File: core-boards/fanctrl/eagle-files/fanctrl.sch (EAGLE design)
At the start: 31 parts, among them J1 3-PIN_2MM-H, U1 MCP9701T-E/TT

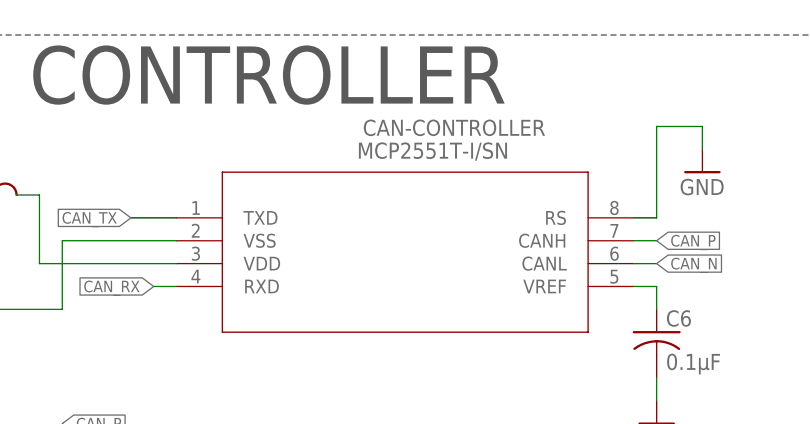
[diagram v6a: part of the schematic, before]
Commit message: Change CAN controller name to MCP2551.
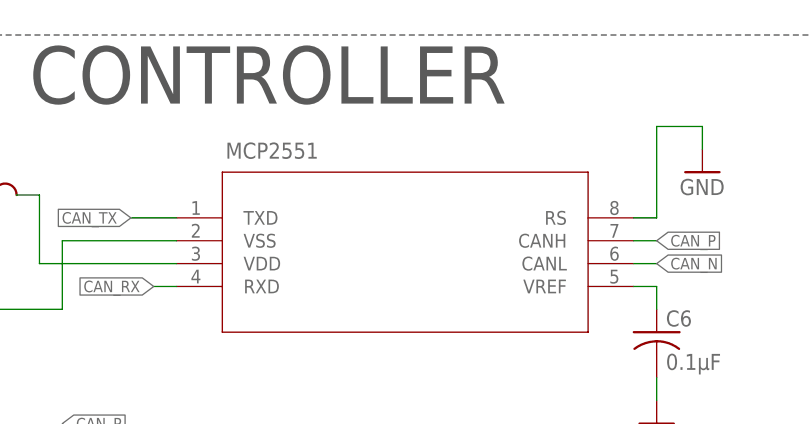
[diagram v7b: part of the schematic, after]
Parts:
- renumbered CAN-CONTROLLER to MCP2551
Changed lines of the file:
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@@
 <part name="P+6" library="supply1" library_urn="urn:adsk.eagle:library:371" deviceset="+5V" device=""/>
 <part name="GND11" library="supply1" library_urn="urn:adsk.eagle:library:371" deviceset="GND" device=""/>
-<part name="CAN-CONTROLLER" library="IGVC-Microcontroller" deviceset="MCP2551T-I/SN" device=""/>
+<part name="MCP2551" library="IGVC-Microcontroller" deviceset="MCP2551T-I/SN" device=""/>
 <part name="C5" library="rcl" library_urn="urn:adsk.eagle:library:334" deviceset="C-US" device="C0603" package3d_urn="urn:adsk.eagle:package:23616/2" value="0.1µF"/>
 <part name="GND12" library="supply1" library_urn="urn:adsk.eagle:library:371" deviceset="GND" device=""/>
@@
 <attribute name="VALUE" x="43.18" y="165.1" size="1.778" layer="96"/>
 </instance>
-<instance part="CAN-CONTROLLER" gate="A" x="190.5" y="187.96" smashed="yes">
-<attribute name="NAME" x="213.7156" y="197.0786" size="1.778" layer="95" rot="SR0"/>
-<attribute name="VALUE" x="213.0806" y="194.5386" size="1.778" layer="96" rot="SR0"/>
+<instance part="MCP2551" gate="A" x="190.5" y="187.96" smashed="yes">
+<attribute name="NAME" x="198.4756" y="194.5386" size="1.778" layer="95" rot="SR0"/>
 </instance>
 <instance part="C5" gate="G$1" x="162.56" y="185.42" smashed="yes">
@@
 </segment>
 <segment>
-<pinref part="CAN-CONTROLLER" gate="A" pin="VSS"/>
+<pinref part="MCP2551" gate="A" pin="VSS"/>
 <wire x1="193.04" y1="185.42" x2="180.34" y2="185.42" width="0.1524" layer="91"/>
 <wire x1="180.34" y1="185.42" x2="180.34" y2="177.8" width="0.1524" layer="91"/>
@@
 </segment>
 <segment>
-<pinref part="CAN-CONTROLLER" gate="A" pin="RS"/>
+<pinref part="MCP2551" gate="A" pin="RS"/>
 <wire x1="243.84" y1="187.96" x2="246.38" y2="187.96" width="0.1524" layer="91"/>
 <wire x1="246.38" y1="187.96" x2="246.38" y2="198.12" width="0.1524" layer="91"/>
@@
 <net name="VREF" class="0">
 <segment>
-<pinref part="CAN-CONTROLLER" gate="A" pin="VREF"/>
+<pinref part="MCP2551" gate="A" pin="VREF"/>
 <wire x1="243.84" y1="180.34" x2="246.38" y2="180.34" width="0.1524" layer="91"/>
 <wire x1="246.38" y1="180.34" x2="246.38" y2="177.8" width="0.1524" layer="91"/>
@@
 <net name="CAN_P" class="0">
 <segment>
-<pinref part="CAN-CONTROLLER" gate="A" pin="CANH"/>
+<pinref part="MCP2551" gate="A" pin="CANH"/>
 <wire x1="243.84" y1="185.42" x2="246.38" y2="185.42" width="0.1524" layer="91"/>
 <label x="246.38" y="185.42" size="1.27" layer="95" font="vector" xref="yes"/>
@@
 <net name="CAN_N" class="0">
 <segment>
-<pinref part="CAN-CONTROLLER" gate="A" pin="CANL"/>
+<pinref part="MCP2551" gate="A" pin="CANL"/>
 <wire x1="243.84" y1="182.88" x2="246.38" y2="182.88" width="0.1524" layer="91"/>
 <label x="246.38" y="182.88" size="1.27" layer="95" font="vector" xref="yes"/>
@@
 <net name="CAN_TX" class="0">
 <segment>
-<pinref part="CAN-CONTROLLER" gate="A" pin="TXD"/>
+<pinref part="MCP2551" gate="A" pin="TXD"/>
 <wire x1="193.04" y1="187.96" x2="187.96" y2="187.96" width="0.1524" layer="91"/>
 <label x="187.96" y="187.96" size="1.27" layer="95" font="vector" rot="R180" xref="yes"/>
@@
 <net name="CAN_RX" class="0">
 <segment>
-<pinref part="CAN-CONTROLLER" gate="A" pin="RXD"/>
+<pinref part="MCP2551" gate="A" pin="RXD"/>
 <wire x1="193.04" y1="180.34" x2="190.5" y2="180.34" width="0.1524" layer="91"/>
 <label x="190.5" y="180.34" size="1.27" layer="95" font="vector" rot="R180" xref="yes"/>
@@
 <net name="+5V_UNFUSED" class="0">
 <segment>
-<pinref part="CAN-CONTROLLER" gate="A" pin="VDD"/>
+<pinref part="MCP2551" gate="A" pin="VDD"/>
 <wire x1="193.04" y1="182.88" x2="177.8" y2="182.88" width="0.1524" layer="91"/>
 <wire x1="177.8" y1="182.88" x2="177.8" y2="190.5" width="0.1524" layer="91"/>

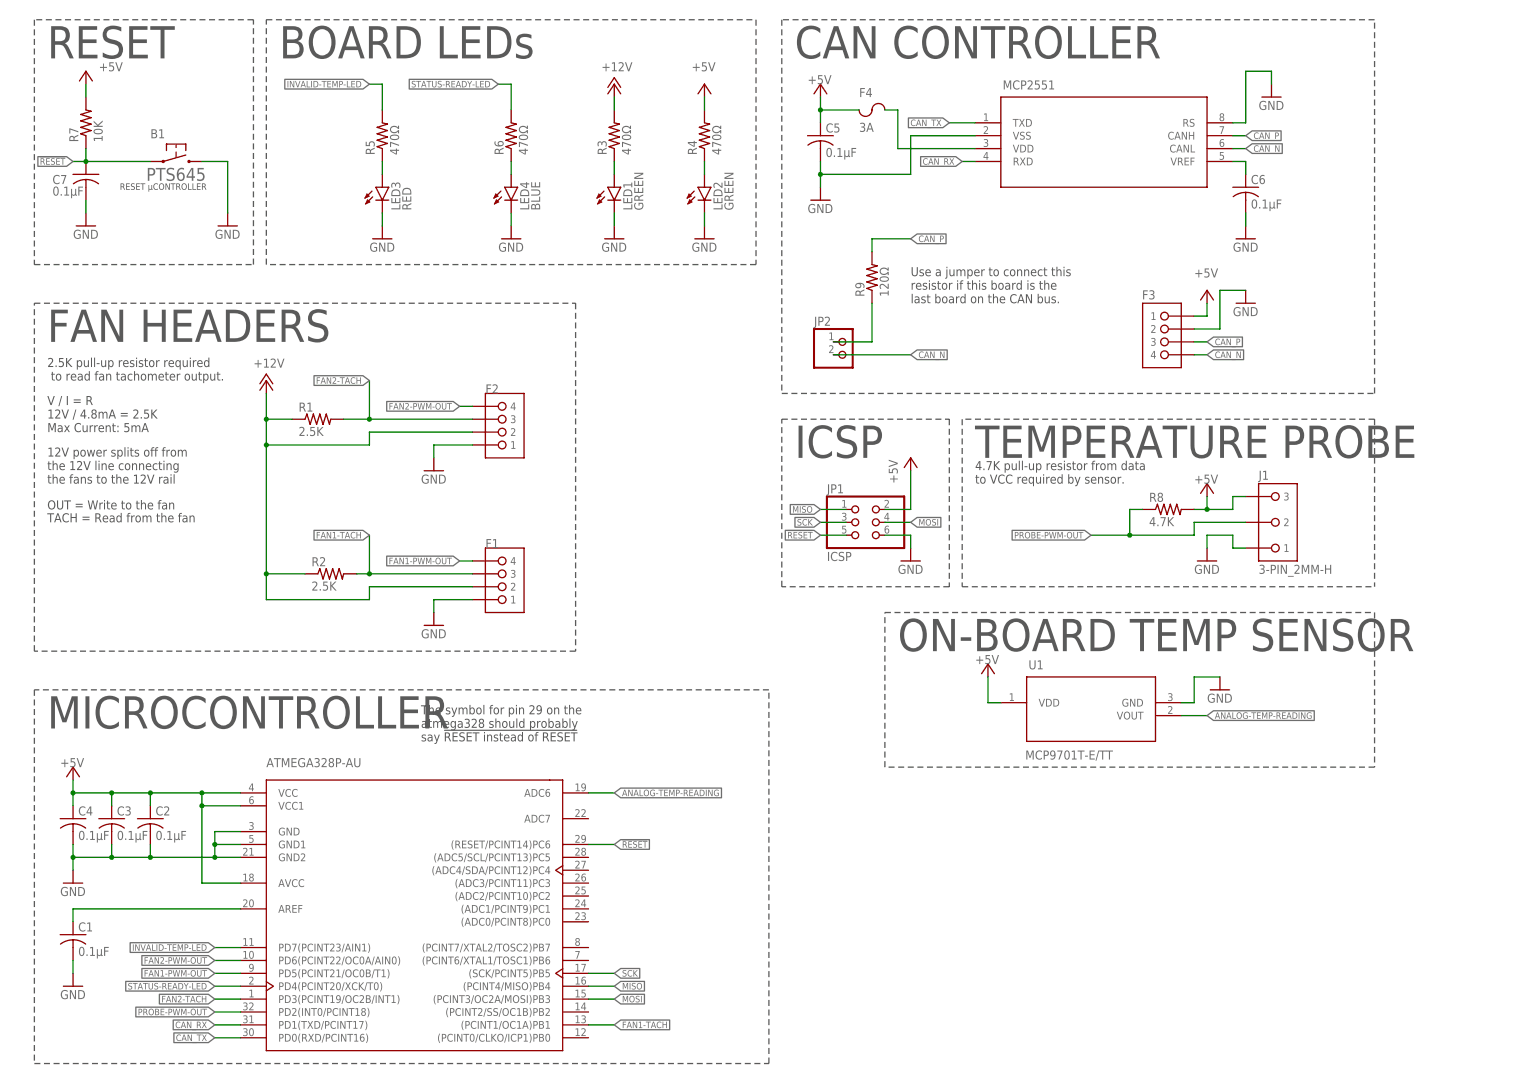
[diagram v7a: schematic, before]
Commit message: Connect fan tachometer lines to interupt pins.
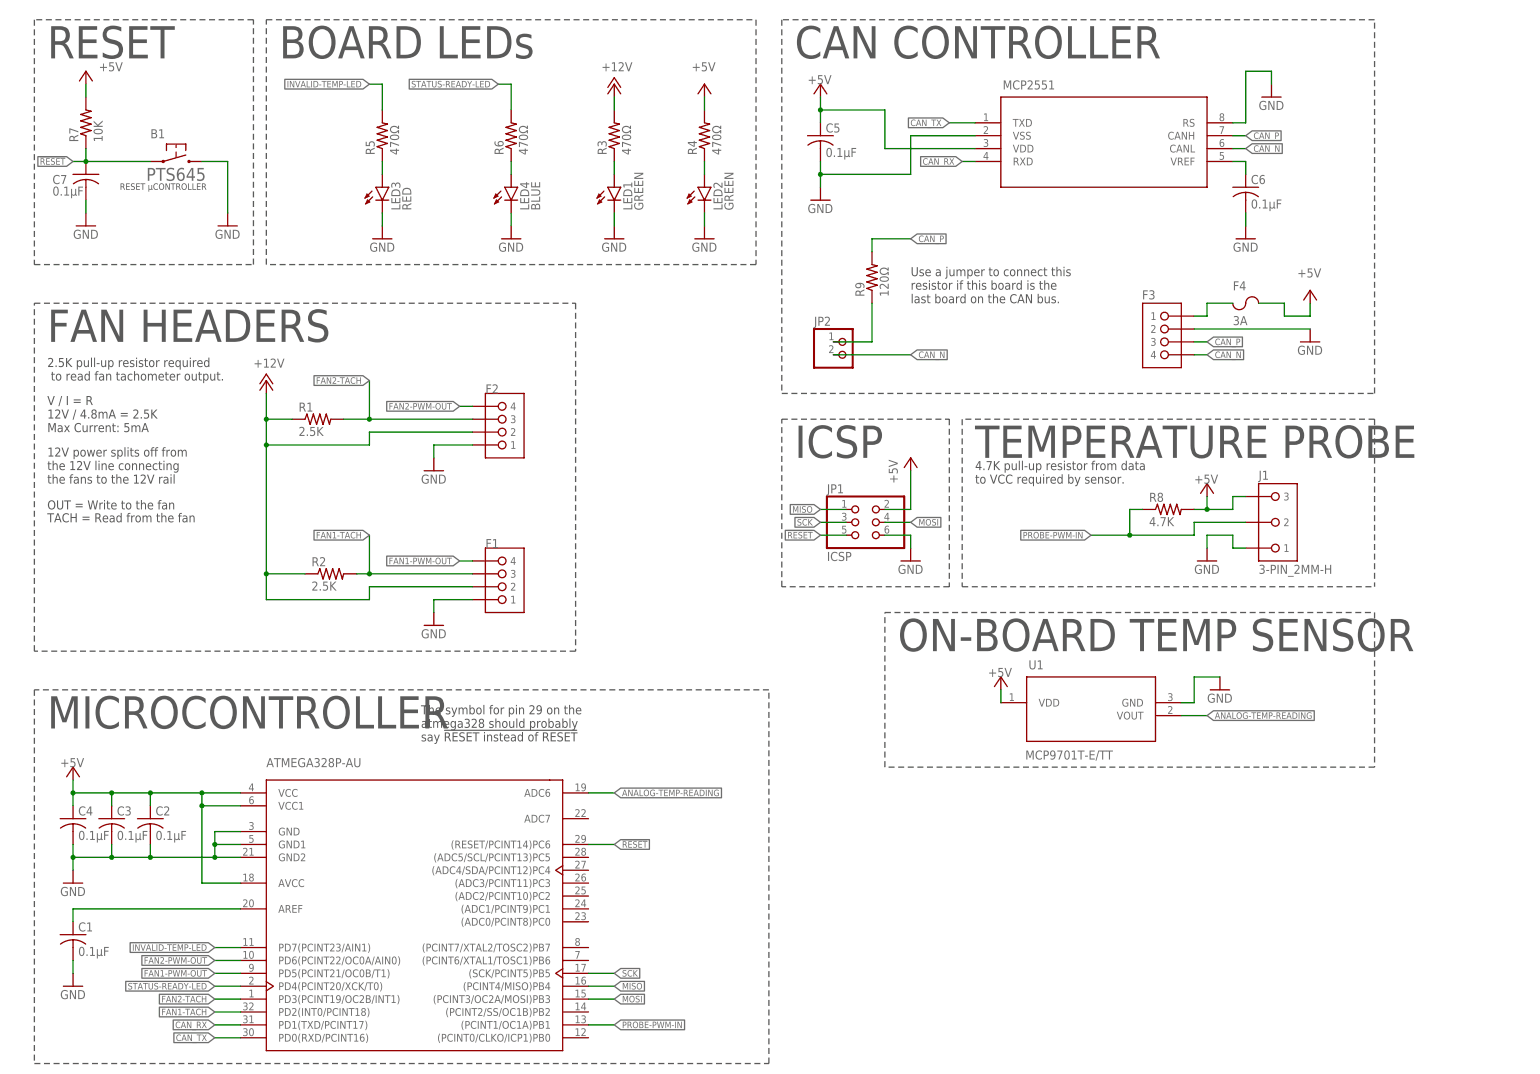
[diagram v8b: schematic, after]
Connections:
- removed net +5V_UNFUSED: F4.2, MCP2551.VDD
- removed net PROBE-PWM-OUT: ATMEGA328.PD2(INT0/PCINT18), J1.2, R8.1
- new net +5_UNFUSED: F3.1, F4.1
- new net PROBE-PWM-IN: ATMEGA328.(PCINT1/OC1A)PB1, J1.2, R8.1
- net +5V: now also F4.2, MCP2551.VDD; no longer F3.1, F4.1
- net FAN1-TACH: now also ATMEGA328.PD2(INT0/PCINT18); no longer ATMEGA328.(PCINT1/OC1A)PB1
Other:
- moved on the sheet: F4
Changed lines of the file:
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@@
 <attribute name="VALUE" x="236.22" y="116.84" size="1.778" layer="96"/>
 </instance>
-<instance part="P+4" gate="1" x="195.58" y="81.28" smashed="yes">
-<attribute name="VALUE" x="193.04" y="81.28" size="1.778" layer="96"/>
+<instance part="P+4" gate="1" x="198.12" y="78.74" smashed="yes">
+<attribute name="VALUE" x="195.58" y="78.74" size="1.778" layer="96"/>
 </instance>
 <instance part="P+5" gate="1" x="15.24" y="60.96" smashed="yes">
@@
 <attribute name="VALUE" x="248.92" y="190.5" size="1.778" layer="96"/>
 </instance>
-<instance part="GND15" gate="1" x="246.38" y="152.4" smashed="yes">
-<attribute name="VALUE" x="243.84" y="149.86" size="1.778" layer="96"/>
-</instance>
-<instance part="P+9" gate="1" x="238.76" y="154.94" smashed="yes">
-<attribute name="VALUE" x="236.22" y="157.48" size="1.778" layer="96"/>
+<instance part="GND15" gate="1" x="259.08" y="144.78" smashed="yes">
+<attribute name="VALUE" x="256.54" y="142.24" size="1.778" layer="96"/>
+</instance>
+<instance part="P+9" gate="1" x="259.08" y="154.94" smashed="yes">
+<attribute name="VALUE" x="256.54" y="157.48" size="1.778" layer="96"/>
 </instance>
 <instance part="R7" gate="G$1" x="17.78" y="187.96" smashed="yes" rot="R90">
@@
 <attribute name="VALUE" x="161.29" y="137.16" size="1.778" layer="96"/>
 </instance>
-<instance part="F4" gate="G$1" x="172.72" y="190.5" smashed="yes">
-<attribute name="NAME" x="170.18" y="193.04" size="1.778" layer="95"/>
-<attribute name="VALUE" x="170.18" y="187.96" size="1.778" layer="96" align="top-left"/>
+<instance part="F4" gate="G$1" x="246.38" y="152.4" smashed="yes">
+<attribute name="NAME" x="243.84" y="154.94" size="1.778" layer="95"/>
+<attribute name="VALUE" x="243.84" y="149.86" size="1.778" layer="96" align="top-left"/>
 </instance>
 </instances>
@@
 </segment>
 <segment>
-<wire x1="236.22" y1="147.32" x2="241.3" y2="147.32" width="0.1524" layer="91"/>
-<wire x1="241.3" y1="147.32" x2="241.3" y2="154.94" width="0.1524" layer="91"/>
 <pinref part="GND15" gate="1" pin="GND"/>
-<wire x1="241.3" y1="154.94" x2="246.38" y2="154.94" width="0.1524" layer="91"/>
+<wire x1="236.22" y1="147.32" x2="259.08" y2="147.32" width="0.1524" layer="91"/>
 <pinref part="F3" gate="G$1" pin="2"/>
 </segment>
@@
 <pinref part="P+4" gate="1" pin="+5V"/>
 <pinref part="U1" gate="MCP9701" pin="VDD"/>
-<wire x1="198.12" y1="73.66" x2="195.58" y2="73.66" width="0.1524" layer="91"/>
-<wire x1="195.58" y1="73.66" x2="195.58" y2="78.74" width="0.1524" layer="91"/>
+<wire x1="198.12" y1="73.66" x2="198.12" y2="76.2" width="0.1524" layer="91"/>
 </segment>
 <segment>
@@
 <pinref part="C5" gate="G$1" pin="1"/>
 <wire x1="162.56" y1="187.96" x2="162.56" y2="190.5" width="0.1524" layer="91"/>
-<pinref part="F4" gate="G$1" pin="1"/>
 <wire x1="162.56" y1="190.5" x2="162.56" y2="193.04" width="0.1524" layer="91"/>
-<wire x1="170.18" y1="190.5" x2="162.56" y2="190.5" width="0.1524" layer="91"/>
+<wire x1="162.56" y1="190.5" x2="175.26" y2="190.5" width="0.1524" layer="91"/>
 <junction x="162.56" y="190.5"/>
-</segment>
-<segment>
-<wire x1="236.22" y1="149.86" x2="238.76" y2="149.86" width="0.1524" layer="91"/>
-<wire x1="238.76" y1="149.86" x2="238.76" y2="152.4" width="0.1524" layer="91"/>
-<pinref part="P+9" gate="1" pin="+5V"/>
-<pinref part="F3" gate="G$1" pin="1"/>
+<wire x1="175.26" y1="190.5" x2="175.26" y2="182.88" width="0.1524" layer="91"/>
+<pinref part="MCP2551" gate="A" pin="VDD"/>
+<wire x1="175.26" y1="182.88" x2="193.04" y2="182.88" width="0.1524" layer="91"/>
 </segment>
 <segment>
@@
 <pinref part="P+10" gate="1" pin="+5V"/>
 </segment>
+<segment>
+<pinref part="P+9" gate="1" pin="+5V"/>
+<wire x1="259.08" y1="152.4" x2="259.08" y2="149.86" width="0.1524" layer="91"/>
+<wire x1="259.08" y1="149.86" x2="254" y2="149.86" width="0.1524" layer="91"/>
+<pinref part="F4" gate="G$1" pin="2"/>
+<wire x1="248.92" y1="152.4" x2="254" y2="152.4" width="0.1524" layer="91"/>
+<wire x1="254" y1="152.4" x2="254" y2="149.86" width="0.1524" layer="91"/>
+</segment>
 </net>
 <net name="ANALOG-TEMP-READING" class="0">
@@
 </net>
 <net name="FAN1-TACH" class="0">
-<segment>
-<pinref part="ATMEGA328" gate="G$1" pin="(PCINT1/OC1A)PB1"/>
-<wire x1="116.84" y1="10.16" x2="121.92" y2="10.16" width="0.1524" layer="91"/>
-<label x="121.92" y="10.16" size="1.27" layer="95" font="vector" xref="yes"/>
-</segment>
 <segment>
 <pinref part="F1" gate="G$1" pin="3"/>
@@
 <label x="73.66" y="106.68" size="1.27" layer="95" font="vector" rot="R180" xref="yes"/>
 </segment>
+<segment>
+<pinref part="ATMEGA328" gate="G$1" pin="PD2(INT0/PCINT18)"/>
+<wire x1="48.26" y1="12.7" x2="43.18" y2="12.7" width="0.1524" layer="91"/>
+<label x="43.18" y="12.7" size="1.27" layer="95" font="vector" rot="R180" xref="yes"/>
+</segment>
 </net>
 <net name="FAN2-PWM-OUT" class="0">
@@
 </segment>
 </net>
-<net name="PROBE-PWM-OUT" class="0">
+<net name="PROBE-PWM-IN" class="0">
 <segment>
 <label x="215.9" y="106.68" size="1.27" layer="95" font="vector" rot="R180" xref="yes"/>
@@
 </segment>
 <segment>
-<pinref part="ATMEGA328" gate="G$1" pin="PD2(INT0/PCINT18)"/>
-<wire x1="48.26" y1="12.7" x2="43.18" y2="12.7" width="0.1524" layer="91"/>
-<label x="43.18" y="12.7" size="1.27" layer="95" font="vector" rot="R180" xref="yes"/>
+<pinref part="ATMEGA328" gate="G$1" pin="(PCINT1/OC1A)PB1"/>
+<wire x1="116.84" y1="10.16" x2="121.92" y2="10.16" width="0.1524" layer="91"/>
+<label x="121.92" y="10.16" size="1.27" layer="95" font="vector" xref="yes"/>
 </segment>
 </net>
@@
 </segment>
 </net>
-<net name="+5V_UNFUSED" class="0">
-<segment>
-<pinref part="MCP2551" gate="A" pin="VDD"/>
-<wire x1="193.04" y1="182.88" x2="177.8" y2="182.88" width="0.1524" layer="91"/>
-<wire x1="177.8" y1="182.88" x2="177.8" y2="190.5" width="0.1524" layer="91"/>
-<pinref part="F4" gate="G$1" pin="2"/>
-<wire x1="177.8" y1="190.5" x2="175.26" y2="190.5" width="0.1524" layer="91"/>
-</segment>
-</net>
+<net name="+5_UNFUSED" class="0">
+<segment>
+<wire x1="236.22" y1="149.86" x2="238.76" y2="149.86" width="0.1524" layer="91"/>
+<pinref part="F3" gate="G$1" pin="1"/>
+<wire x1="238.76" y1="149.86" x2="238.76" y2="152.4" width="0.1524" layer="91"/>
+<pinref part="F4" gate="G$1" pin="1"/>
+<wire x1="238.76" y1="152.4" x2="243.84" y2="152.4" width="0.1524" layer="91"/>
+</segment>
+</net>
